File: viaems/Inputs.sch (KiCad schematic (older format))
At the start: 63 parts, among them J18 Conn_01x06, U12 MPXA6115A, U13 MPXA6115A, U14 LM2940, U15 AD7888

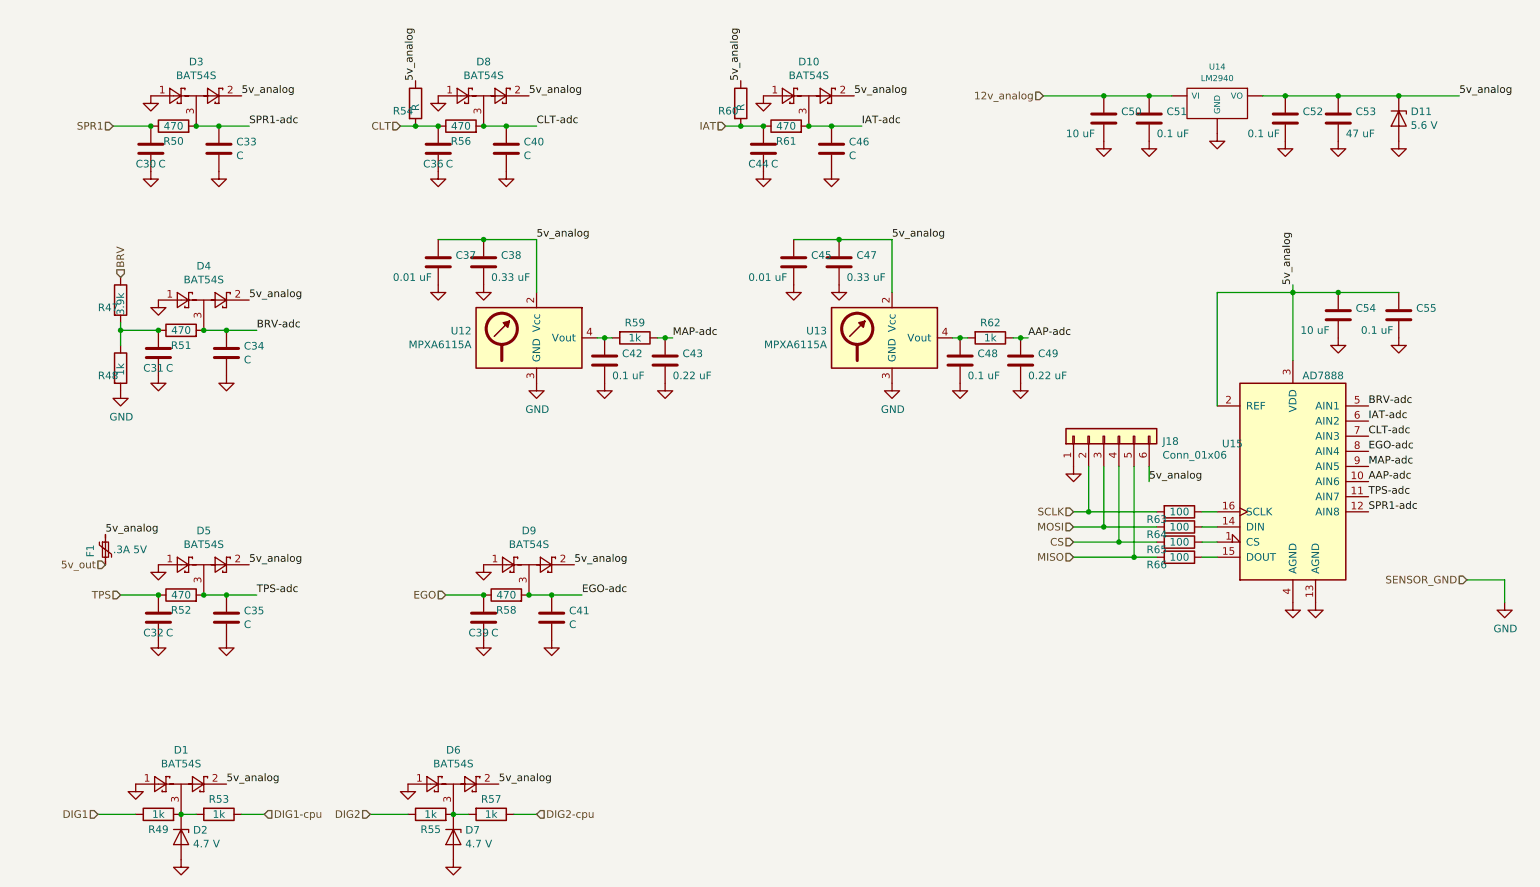
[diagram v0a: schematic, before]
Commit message: More progress. Calling schematic complete, board partially routed
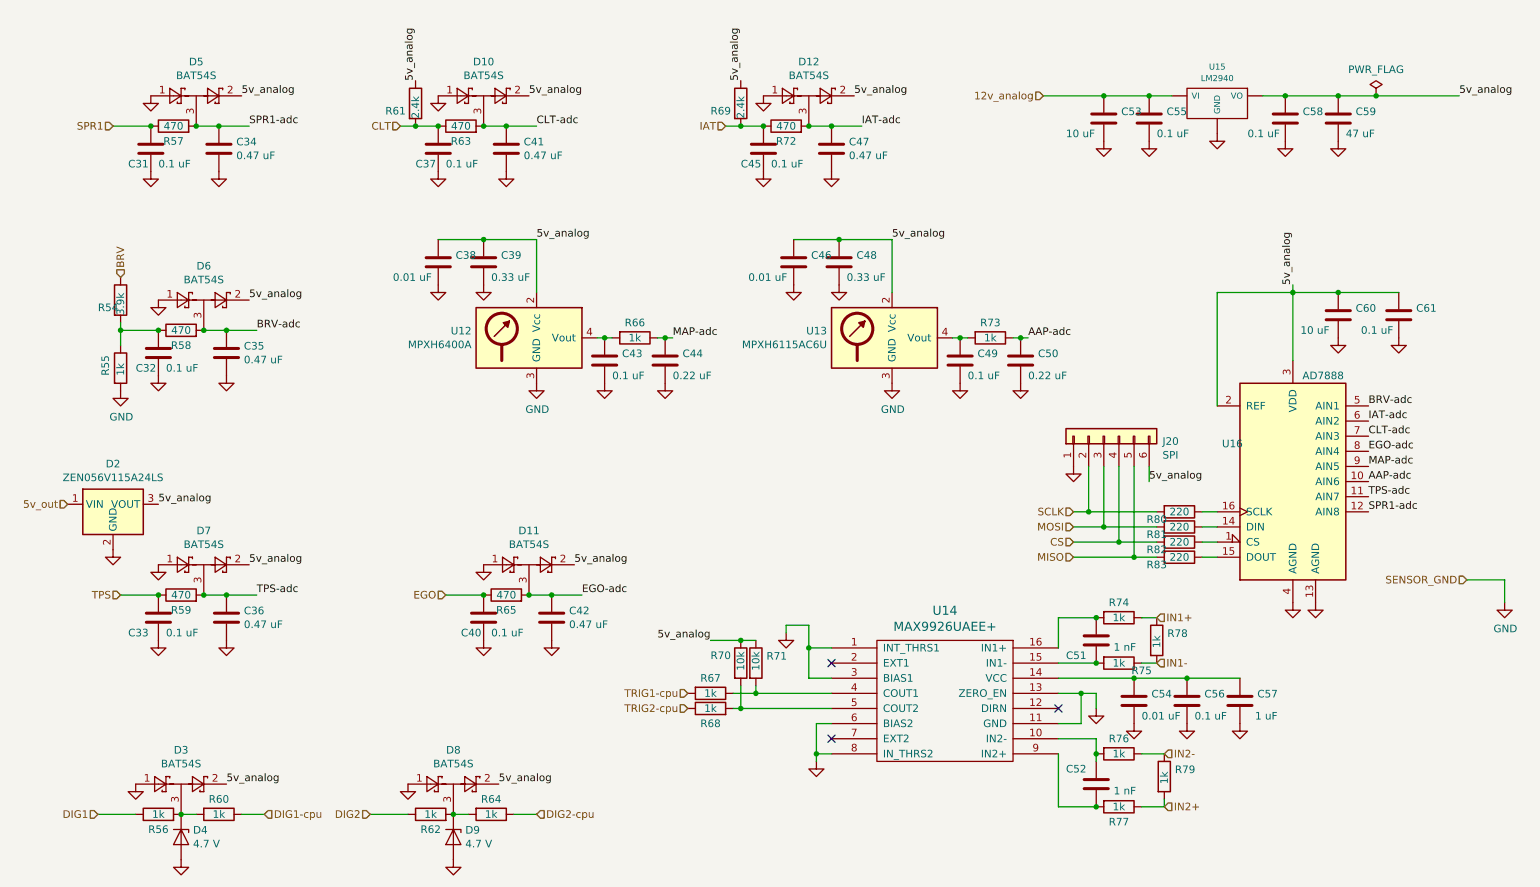
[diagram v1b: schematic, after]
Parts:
- removed D11: 5.6 V, symbol Device:D_Zener
- removed F1: .3A 5V, symbol Device:Polyfuse_Small
- added C51, C52: 1 nF, Capacitor_SMD:C_0805_2012Metric_Pad1.15x1.40mm_HandSolder, symbol Device:C
- added C54: 0.01 uF, Capacitor_SMD:C_0805_2012Metric_Pad1.15x1.40mm_HandSolder, symbol Device:C
- added C56: 0.1 uF, Capacitor_SMD:C_0805_2012Metric_Pad1.15x1.40mm_HandSolder, symbol Device:C
- added C57: 1 uF, Capacitor_SMD:C_0805_2012Metric_Pad1.15x1.40mm_HandSolder, symbol Device:C
- added D2: ZEN056V115A24LS, Diode_SMD:Littelfuse_PolyZen-LS, symbol Power_Protection:ZEN056V115A24LS
- added R67, R68, R74, R75, R76, R77: 1k, Resistor_SMD:R_0805_2012Metric_Pad1.15x1.40mm_HandSolder, symbol Device:R
- added R70, R71: 10k, Resistor_SMD:R_0805_2012Metric_Pad1.15x1.40mm_HandSolder, symbol Device:R
- added R78, R79: 1k, Resistor_THT:R_Axial_DIN0207_L6.3mm_D2.5mm_P2.54mm_Vertical, symbol Device:R
- added U14: MAX9926UAEE+, Package_SO:QSOP-16_3.9x4.9mm_P0.635mm, symbol viaems:MAX9926UAEE+
- C31: renamed from C30; value C -> 0.1 uF; footprint (none) -> Capacitor_SMD:C_0805_2012Metric_Pad1.15x1.40mm_HandSolder; Digikey-Part (none) -> 478-10836-1-ND; Notes (none) -> 35V
- C32: renamed from C31; value C -> 0.1 uF; footprint (none) -> Capacitor_SMD:C_0805_2012Metric_Pad1.15x1.40mm_HandSolder; Digikey-Part (none) -> 478-10836-1-ND; Notes (none) -> 35V
- C33: renamed from C32; value C -> 0.1 uF; footprint (none) -> Capacitor_SMD:C_0805_2012Metric_Pad1.15x1.40mm_HandSolder; Digikey-Part (none) -> 478-10836-1-ND; Notes (none) -> 35V
- C34: renamed from C33; value C -> 0.47 uF; footprint (none) -> Capacitor_SMD:C_0805_2012Metric_Pad1.15x1.40mm_HandSolder
- C35: renamed from C34; value C -> 0.47 uF; footprint (none) -> Capacitor_SMD:C_0805_2012Metric_Pad1.15x1.40mm_HandSolder
- C36: renamed from C35; value C -> 0.47 uF; footprint (none) -> Capacitor_SMD:C_0805_2012Metric_Pad1.15x1.40mm_HandSolder
- C37: renamed from C36; value C -> 0.1 uF; footprint (none) -> Capacitor_SMD:C_0805_2012Metric_Pad1.15x1.40mm_HandSolder; Digikey-Part (none) -> 478-10836-1-ND; Notes (none) -> 35V
- C38: renamed from C37; footprint (none) -> Capacitor_SMD:C_0805_2012Metric_Pad1.15x1.40mm_HandSolder
- C39: renamed from C38; footprint (none) -> Capacitor_SMD:C_0805_2012Metric_Pad1.15x1.40mm_HandSolder
- C40: renamed from C39; value C -> 0.1 uF; footprint (none) -> Capacitor_SMD:C_0805_2012Metric_Pad1.15x1.40mm_HandSolder; Digikey-Part (none) -> 478-10836-1-ND; Notes (none) -> 35V
- C41: renamed from C40; value C -> 0.47 uF; footprint (none) -> Capacitor_SMD:C_0805_2012Metric_Pad1.15x1.40mm_HandSolder
- C42: renamed from C41; value C -> 0.47 uF; footprint (none) -> Capacitor_SMD:C_0805_2012Metric_Pad1.15x1.40mm_HandSolder
- C43: renamed from C42; footprint (none) -> Capacitor_SMD:C_0805_2012Metric_Pad1.15x1.40mm_HandSolder
- C44: renamed from C43; footprint (none) -> Capacitor_SMD:C_0805_2012Metric_Pad1.15x1.40mm_HandSolder
- C45: renamed from C44; value C -> 0.1 uF; footprint (none) -> Capacitor_SMD:C_0805_2012Metric_Pad1.15x1.40mm_HandSolder; Digikey-Part (none) -> 478-10836-1-ND; Notes (none) -> 35V
- C46: renamed from C45; footprint (none) -> Capacitor_SMD:C_0805_2012Metric_Pad1.15x1.40mm_HandSolder
- C47: renamed from C46; value C -> 0.47 uF; footprint (none) -> Capacitor_SMD:C_0805_2012Metric_Pad1.15x1.40mm_HandSolder
- C48: renamed from C47; footprint (none) -> Capacitor_SMD:C_0805_2012Metric_Pad1.15x1.40mm_HandSolder
- C49: renamed from C48; footprint (none) -> Capacitor_SMD:C_0805_2012Metric_Pad1.15x1.40mm_HandSolder
- C50: renamed from C49; footprint (none) -> Capacitor_SMD:C_0805_2012Metric_Pad1.15x1.40mm_HandSolder
- C53: renamed from C50; footprint (none) -> Capacitor_SMD:C_1206_3216Metric_Pad1.42x1.75mm_HandSolder; Digikey-Part (none) -> 445-14799-1-ND; Notes (none) -> 35V
- C55: renamed from C51; footprint (none) -> Capacitor_SMD:C_0805_2012Metric_Pad1.15x1.40mm_HandSolder
- C58: renamed from C52; footprint (none) -> Capacitor_SMD:C_0805_2012Metric_Pad1.15x1.40mm_HandSolder
- C59: renamed from C53; footprint (none) -> Capacitor_SMD:C_1206_3216Metric_Pad1.42x1.75mm_HandSolder; Digikey-Part (none) -> 478-9009-1-ND; Notes (none) -> Tantalum
- C60: renamed from C54; footprint (none) -> Capacitor_SMD:C_0805_2012Metric_Pad1.15x1.40mm_HandSolder; Digikey-Part (none) -> 587-3417-1-ND
- C61: renamed from C55; footprint (none) -> Capacitor_SMD:C_0805_2012Metric_Pad1.15x1.40mm_HandSolder
- D10: renamed from D8; footprint Package_TO_SOT_SMD:SOT-23 -> Package_TO_SOT_SMD:SOT-23_Handsoldering; Digikey-Part (none) -> BAT54SLT1GOSCT-ND
- D11: renamed from D9; footprint Package_TO_SOT_SMD:SOT-23 -> Package_TO_SOT_SMD:SOT-23_Handsoldering; Digikey-Part (none) -> BAT54SLT1GOSCT-ND
- D12: renamed from D10; footprint Package_TO_SOT_SMD:SOT-23 -> Package_TO_SOT_SMD:SOT-23_Handsoldering; Digikey-Part (none) -> BAT54SLT1GOSCT-ND
- D3: renamed from D1; footprint Package_TO_SOT_SMD:SOT-23 -> Package_TO_SOT_SMD:SOT-23_Handsoldering; Digikey-Part (none) -> BAT54SLT1GOSCT-ND
- D4: renamed from D2; footprint (none) -> Diode_SMD:D_0603_1608Metric_Pad1.05x0.95mm_HandSolder; Digikey-Part (none) -> 478-10836-1-ND
- D5: renamed from D3; footprint Package_TO_SOT_SMD:SOT-23 -> Package_TO_SOT_SMD:SOT-23_Handsoldering; Digikey-Part (none) -> BAT54SLT1GOSCT-ND
- D6: renamed from D4; footprint Package_TO_SOT_SMD:SOT-23 -> Package_TO_SOT_SMD:SOT-23_Handsoldering; Digikey-Part (none) -> BAT54SLT1GOSCT-ND
- D7: renamed from D5; footprint Package_TO_SOT_SMD:SOT-23 -> Package_TO_SOT_SMD:SOT-23_Handsoldering; Digikey-Part (none) -> BAT54SLT1GOSCT-ND
- D8: renamed from D6; footprint Package_TO_SOT_SMD:SOT-23 -> Package_TO_SOT_SMD:SOT-23_Handsoldering; Digikey-Part (none) -> BAT54SLT1GOSCT-ND
- D9: renamed from D7; footprint (none) -> Diode_SMD:D_0805_2012Metric_Pad1.15x1.40mm_HandSolder; Digikey-Part (none) -> 478-10836-1-ND
- J20: renamed from J18; value Conn_01x06 -> SPI; footprint (none) -> Connector_PinHeader_2.54mm:PinHeader_1x06_P2.54mm_Vertical
- R54: renamed from R47; footprint (none) -> Resistor_SMD:R_0805_2012Metric_Pad1.15x1.40mm_HandSolder
- R55: renamed from R48; footprint (none) -> Resistor_SMD:R_0805_2012Metric_Pad1.15x1.40mm_HandSolder
- R56: renamed from R49; footprint (none) -> Resistor_SMD:R_0805_2012Metric_Pad1.15x1.40mm_HandSolder
- R57: renamed from R50; footprint (none) -> Resistor_SMD:R_0805_2012Metric_Pad1.15x1.40mm_HandSolder
- R58: renamed from R51; footprint (none) -> Resistor_SMD:R_0805_2012Metric_Pad1.15x1.40mm_HandSolder
- R59: renamed from R52; footprint (none) -> Resistor_SMD:R_0805_2012Metric_Pad1.15x1.40mm_HandSolder
- R60: renamed from R53; footprint (none) -> Resistor_SMD:R_0805_2012Metric_Pad1.15x1.40mm_HandSolder
- R61: renamed from R54; value R -> 2.4k; footprint (none) -> Resistor_SMD:R_0805_2012Metric_Pad1.15x1.40mm_HandSolder
- R62: renamed from R55; footprint (none) -> Resistor_SMD:R_0805_2012Metric_Pad1.15x1.40mm_HandSolder
- R63: renamed from R56; footprint (none) -> Resistor_SMD:R_0805_2012Metric_Pad1.15x1.40mm_HandSolder
- R64: renamed from R57; footprint (none) -> Resistor_SMD:R_0805_2012Metric_Pad1.15x1.40mm_HandSolder
- R65: renamed from R58; footprint (none) -> Resistor_SMD:R_0805_2012Metric_Pad1.15x1.40mm_HandSolder
- R66: renamed from R59; footprint (none) -> Resistor_SMD:R_0805_2012Metric_Pad1.15x1.40mm_HandSolder
- R69: renamed from R60; value R -> 2.4k; footprint (none) -> Resistor_SMD:R_0805_2012Metric_Pad1.15x1.40mm_HandSolder
- R72: renamed from R61; footprint (none) -> Resistor_SMD:R_0805_2012Metric_Pad1.15x1.40mm_HandSolder
- R73: renamed from R62; footprint (none) -> Resistor_SMD:R_0805_2012Metric_Pad1.15x1.40mm_HandSolder
- R80: renamed from R63; value 100 -> 220; footprint (none) -> Resistor_SMD:R_0805_2012Metric_Pad1.15x1.40mm_HandSolder
- R81: renamed from R64; value 100 -> 220; footprint (none) -> Resistor_SMD:R_0805_2012Metric_Pad1.15x1.40mm_HandSolder
- R82: renamed from R65; value 100 -> 220; footprint (none) -> Resistor_SMD:R_0805_2012Metric_Pad1.15x1.40mm_HandSolder
- R83: renamed from R66; value 100 -> 220; footprint (none) -> Resistor_SMD:R_0805_2012Metric_Pad1.15x1.40mm_HandSolder
- U12: value MPXA6115A -> MPXH6400A; footprint (none) -> Sensor_Pressure:Freescale_98ARH99089A; Digikey-Part (none) -> MPXH6400AC6T1CT-ND
- U13: value MPXA6115A -> MPXH6115AC6U; footprint (none) -> Sensor_Pressure:Freescale_98ARH99089A; Digikey-Part (none) -> MPXH6115AC6U-ND
- U15: renamed from U14; footprint (none) -> Package_TO_SOT_THT:TO-220-3_Horizontal_TabDown
- U16: renamed from U15; footprint (none) -> Package_SO:SOIC-16_3.9x9.9mm_P1.27mm; Digikey-Part (none) -> AD7888ARZ-REEL7CT-ND
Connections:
- net 5v_analog: now also D2.3 (VOUT), R70.1, R71.1
- net 5v_out: now also D2.1 (VIN)
- net GND: now also C54.2, C56.2, C57.2, D2.2 (GND), U14.1 (INT_THRS1), U14.11 (GND), U14.13 (ZERO_EN), U14.3 (BIAS1), U14.6 (BIAS2), U14.8 (IN_THRS2)
- new net: C52.1, R76.2, U14.10 (IN2-)
- new net: C54.1, C56.1, C57.1, U14.14 (VCC)
- new net: C51.2, R75.2, U14.15 (IN1-)
- new net: C51.1, R74.2, U14.16 (IN1+)
- new net: R67.1, R71.2, U14.4 (COUT1)
- new net: R68.2, R70.2, U14.5 (COUT2)
- new net: C52.2, R77.2, U14.9 (IN2+)
- new net IN1+: R74.1, R78.1
- new net IN1-: R75.1, R78.2
- new net IN2+: R77.1, R79.2
- new net IN2-: R76.1, R79.1
- new net TRIG1-cpu: R67.2
- new net TRIG2-cpu: R68.1
- no-connect marks 0 -> 3

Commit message: More routing
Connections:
- net 5v_analog: no longer D3.2, D8.2, J20.6 (Pin_6), R70.1, R71.1
- net CS: now also J20.2 (Pin_2); no longer J20.4 (Pin_4)
- net MISO: now also J20.4 (Pin_4); no longer J20.5 (Pin_5)
- net MOSI: now also J20.5 (Pin_5); no longer J20.3 (Pin_3)
- net SCLK: now also J20.3 (Pin_3); no longer J20.2 (Pin_2)
- net 5v_cpu: now reaches C54.1, C56.1, C57.1, U14.14 (VCC)
- net 5v_cpu: now also D3.2, D8.2, J20.6 (Pin_6), R70.1, R71.1
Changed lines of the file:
@@
 	3700 4900 3450 4900
 Connection ~ 3700 4900
-Text Label 2000 6150 0    50   ~ 0
-5v_analog
 $Comp
 L power:GND #PWR065
@@
 Wire Wire Line
 	2100 6350 2250 6350
-Text Label 3800 6150 0    50   ~ 0
-5v_analog
 $Comp
 L power:GND #PWR076
@@
 Wire Wire Line
 	8450 4650 8550 4650
-Wire Wire Line
-	7600 4350 7700 4350
 $Comp
 L Connector_Generic:Conn_01x06 J20
@@
 	1    0    0    -1
 $EndComp
-Text Label 8100 4150 0    50   ~ 0
-5v_analog
 Wire Wire Line
 	8100 4150 8100 4050
-Wire Wire Line
-	7700 4050 7700 4350
-Connection ~ 7700 4350
-Wire Wire Line
-	7800 4050 7800 4450
-Connection ~ 7800 4450
-Wire Wire Line
-	7800 4450 7600 4450
-Wire Wire Line
-	7700 4350 8150 4350
-Wire Wire Line
-	7800 4450 8150 4450
-Wire Wire Line
-	7600 4550 7900 4550
-Wire Wire Line
-	7600 4650 8000 4650
-Wire Wire Line
-	7900 4050 7900 4550
-Connection ~ 7900 4550
-Wire Wire Line
-	7900 4550 8150 4550
-Wire Wire Line
-	8000 4050 8000 4650
-Connection ~ 8000 4650
-Wire Wire Line
-	8000 4650 8150 4650
 Text HLabel 4050 6350 2    50   Input ~ 0
 DIG2-cpu
@@
 Wire Wire Line
 	5400 5650 5350 5650
-Text Label 5200 5200 2    50   ~ 0
-5v_analog
 Wire Wire Line
 	5200 5200 5400 5200
@@
 Text HLabel 8150 5050 2    50   Input ~ 0
 IN1+
+Text HLabel 5200 5200 0    50   Input ~ 0
+5v_cpu
+Text HLabel 3800 6150 2    50   Input ~ 0
+5v_cpu
+Text HLabel 2000 6150 2    50   Input ~ 0
+5v_cpu
+Text HLabel 8700 5450 2    50   Input ~ 0
+5v_cpu
+Text HLabel 8100 4150 2    50   Input ~ 0
+5v_cpu
+Wire Wire Line
+	7600 4350 7800 4350
+Wire Wire Line
+	7600 4450 8000 4450
+Wire Wire Line
+	7600 4550 7700 4550
+Wire Wire Line
+	7600 4650 7900 4650
+Wire Wire Line
+	7700 4050 7700 4550
+Connection ~ 7700 4550
+Wire Wire Line
+	7700 4550 8150 4550
+Connection ~ 7800 4350
+Wire Wire Line
+	7800 4050 7800 4350
+Wire Wire Line
+	7900 4050 7900 4650
+Connection ~ 7900 4650
+Wire Wire Line
+	7900 4650 8150 4650
+Wire Wire Line
+	7800 4350 8150 4350
+Wire Wire Line
+	8000 4050 8000 4450
+Connection ~ 8000 4450
+Wire Wire Line
+	8000 4450 8150 4450
 $EndSCHEMATC

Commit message: Misc fixes
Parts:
- C34, C35, C36, C41, C42, C47: Digikey-Part (none) -> 1276-6851-1-ND
- C38, C43, C46, C54: Digikey-Part (none) -> 1276-1015-1-ND
- C39, C48: Digikey-Part (none) -> 1276-1123-1-ND
- C44, C50: Digikey-Part (none) -> 1276-1093-1-ND
- C49, C55, C56, C58, C61: Digikey-Part (none) -> 478-10836-1-ND
- C51, C52: Digikey-Part (none) -> 399-1147-1-ND
- C53: Digikey-Part 445-14799-1-ND -> 445-8034-1-ND
- C57: Digikey-Part (none) -> 1276-1066-1-ND
- D2: Digikey-Part (none) -> ZEN056V115A24LSCT-ND
- D4, D9: Digikey-Part 478-10836-1-ND -> (none)
- J20: Digikey-Part (none) -> 732-5319-ND
- R54: Digikey-Part (none) -> P3.9KDACT-ND; Notes (none) -> 0.1%
- R55: Digikey-Part (none) -> P1.0KDACT-ND; Notes (none) -> 0.1%
- R56, R60, R62, R64, R66, R67, R68, R73, R74, R75, R76, R77: Digikey-Part (none) -> RNCP0805FTD1K00CT-ND
- R57, R58, R59, R63, R65, R72: Digikey-Part (none) -> 311-470CRCT-ND
- R61, R69: Digikey-Part (none) -> P2.4KDACT-ND
- R70, R71: Digikey-Part (none) -> RNCF0805DTE10K0CT-ND
- R78, R79: Digikey-Part 478-10836-1-ND -> PPC1.0KW-1CT-ND
- R80, R81, R82, R83: Digikey-Part (none) -> A129741CT-ND
- U15: Digikey-Part (none) -> LM2940T-5.0/NOPB-ND
